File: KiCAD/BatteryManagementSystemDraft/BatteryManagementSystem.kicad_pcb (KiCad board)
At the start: 2 copper layers, 237.5 x 165 mm, 368 parts, among them J2 Conn_01x07_Male, J5 Conn_01x07_Male, J6 Conn_01x07_Male, Q1 Q_NMOS_GDS, Q2 NMOS_PowerPak_SO8, Q3 NMOS_PowerPak_SO8, Q4 NMOS_PowerPak_SO8, Q5 NMOS_PowerPak_SO8, T1 750311880, U1 750312504, U2 LTC3300HLXE-2#PBF, U3 LTC6804HG-1#PBF, U4 LTC6820IMS#PBF, U5 BQ79606APHPTQ1

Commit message: Updated Kicad Files
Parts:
- removed the C1 at (57.9, 160.4)
- removed the C1 at (57.9, 170.9)
- removed the C1 at (57.9, 139.6)
- removed the C1 at (58.0, 181.2)
- removed the C1 at (57.9, 129.2)
- removed the C1 at (57.9, 150.0)
- removed the C10 at (141.3, 92.0)
- removed the C10 at (141.3, 118.7)
- removed the C10 at (141.3, 171.1)
- removed the C10 at (141.3, 65.1)
- removed the C10 at (141.3, 145.2)
- removed the C10 at (141.3, 37.9)
- removed the C11 at (134.5, 52.4)
- removed the C11 at (134.5, 106.0)
- removed the C11 at (134.5, 79.3)
- removed the C11 at (134.5, 132.5)
- removed the C11 at (134.5, 158.4)
- removed the C11 at (134.5, 25.2)
- removed the C12 at (141.9, 52.4)
- removed the C12 at (141.9, 106.0)
- removed the C12 at (141.9, 79.3)
- removed the C12 at (141.9, 132.5)
- removed the C12 at (141.9, 158.4)
- removed the C12 at (141.9, 25.2)
- removed the C13 at (138.2, 79.3)
- removed the C13 at (138.2, 52.4)
- removed the C13 at (138.2, 106.0)
- removed the C13 at (138.2, 158.4)
- removed the C13 at (138.2, 132.5)
- removed the C13 at (138.2, 25.2)
- removed the C14 at (222.3, 85.8)
- removed the C14 at (199.4, 102.2)
- removed the C14 at (222.3, 118.2)
- removed the C14 at (199.4, 134.7)
- removed the C14 at (222.3, 152.1)
- removed the C14 at (199.4, 168.4)
- removed the C15 at (222.3, 89.2)
- removed the C15 at (199.4, 105.6)
- removed the C15 at (222.3, 121.6)
- removed the C15 at (199.4, 138.1)
- removed the C15 at (222.3, 155.5)
- removed the C15 at (199.4, 171.8)
- removed the C16 at (222.3, 92.7)
- removed the C16 at (199.4, 109.0)
- removed the C16 at (222.3, 125.0)
- removed the C16 at (199.4, 141.6)
- removed the C16 at (222.3, 159.0)
- removed the C16 at (199.4, 175.2)
- removed the C17 at (224.7, 97.2)
- removed the C17 at (201.8, 113.6)
- removed the C17 at (224.7, 129.6)
- removed the C17 at (201.8, 146.1)
- removed the C17 at (224.7, 163.5)
- removed the C17 at (201.8, 179.8)
- removed the C18 at (238.4, 94.2)
- removed the C18 at (215.5, 110.6)
- removed the C18 at (238.4, 126.6)
- removed the C18 at (215.5, 143.1)
- removed the C18 at (238.4, 160.5)
- removed the C18 at (215.5, 176.7)
- removed the C19 at (222.8, 80.5)
- removed the C19 at (199.9, 96.9)
- removed the C19 at (222.8, 112.9)
- removed the C19 at (199.9, 129.4)
- removed the C19 at (222.8, 146.8)
- removed the C19 at (199.9, 163.0)
- removed the C2 at (52.6, 129.1)
- removed the C2 at (52.6, 170.8)
- removed the C2 at (52.7, 181.2)
- removed the C2 at (52.6, 150.0)
- removed the C2 at (52.6, 160.4)
- removed the C2 at (52.6, 139.6)
- removed the C20 at (237.4, 91.0)
- removed the C20 at (214.5, 107.4)
- removed the C20 at (237.4, 123.4)
- removed the C20 at (214.5, 139.9)
- removed the C20 at (237.4, 157.3)
- removed the C20 at (214.5, 173.6)
- removed the C21 at (241.5, 91.5)
- removed the C21 at (218.6, 107.9)
- removed the C21 at (241.5, 123.9)
- removed the C21 at (218.6, 140.4)
- removed the C21 at (241.5, 157.8)
- removed the C21 at (218.6, 174.1)
- removed the C22 at (241.5, 84.4)
- removed the C22 at (218.6, 100.8)
- removed the C22 at (241.5, 116.8)
- removed the C22 at (218.6, 133.3)
- removed the C22 at (241.5, 150.7)
- removed the C22 at (218.6, 167.0)
- removed the C23 at (241.5, 88.0)
- removed the C23 at (218.6, 104.3)
- removed the C23 at (241.5, 120.3)
- removed the C23 at (218.6, 136.9)
- removed the C23 at (241.5, 154.3)
- removed the C23 at (218.6, 170.5)
- removed the C3 at (58.5, 126.4)
- removed the C3 at (58.5, 136.8)
- removed the C3 at (58.5, 157.7)
- removed the C3 at (58.5, 178.4)
- removed the C3 at (58.5, 147.3)
- removed the C3 at (58.5, 168.1)
- removed the C4 at (121.1, 46.3)
- removed the C4 at (121.1, 73.4)
- removed the C4 at (121.1, 153.6)
- removed the C4 at (121.1, 100.4)
- removed the C4 at (121.1, 127.0)
- removed the C4 at (121.1, 179.5)
- removed the C5 at (117.5, 73.4)
- removed the C5 at (117.5, 179.5)
- removed the C5 at (117.5, 100.4)
- removed the C5 at (117.5, 127.0)
- removed the C5 at (117.5, 153.6)
- removed the C5 at (117.5, 46.3)
- removed the C6 at (114.0, 73.4)
- removed the C6 at (114.0, 100.4)
- removed the C6 at (114.0, 153.6)
- removed the C6 at (114.0, 127.0)
- removed the C6 at (114.0, 179.5)
- removed the C6 at (114.0, 46.3)
- removed the C7 at (110.3, 50.3)
- removed the C7 at (110.3, 77.3)
- removed the C7 at (110.3, 103.9)
- removed the C7 at (110.3, 130.5)
- removed the C7 at (110.3, 156.4)
- removed the C7 at (110.3, 23.2)
- removed the C8 at (112.8, 64.3)
- removed the C8 at (112.8, 91.2)
- removed the C8 at (112.8, 117.9)
- removed the C8 at (112.8, 144.4)
- removed the C8 at (112.8, 170.3)
- removed the C8 at (112.8, 37.1)
- removed the C9 at (135.4, 69.9)
- removed the C9 at (135.4, 123.5)
- removed the C9 at (135.4, 96.8)
- removed the C9 at (135.4, 150.0)
- removed the C9 at (135.4, 175.9)
- removed the C9 at (135.4, 42.7)
- removed the D1 at (54.9, 139.7)
- removed the D1 at (55.0, 181.3)
- removed the D1 at (54.9, 160.5)
- removed the D1 at (54.9, 129.3)
- removed the D1 at (54.9, 150.1)
- removed the D1 at (54.9, 170.9)
- removed the D2 at (112.4, 94.9)
- removed the D2 at (112.4, 174.0)
- removed the D2 at (112.4, 148.1)
- removed the D2 at (112.4, 40.8)
- removed the D2 at (112.4, 121.6)
- removed the D2 at (112.4, 68.0)
- removed the D3 at (104.9, 57.2)
- removed the D3 at (104.9, 163.2)
- removed the D3 at (104.9, 110.8)
- removed the D3 at (104.9, 84.1)
- removed the D3 at (104.9, 137.3)
- removed the D3 at (104.9, 30.0)
- removed the D4 at (112.8, 59.5)
- removed the D4 at (112.8, 86.4)
- removed the D4 at (112.8, 165.5)
- removed the D4 at (112.8, 113.1)
- removed the D4 at (112.8, 139.6)
- removed the D4 at (112.8, 32.3)
- removed the D5 at (135.4, 92.0)
- removed the D5 at (135.4, 37.9)
- removed the D5 at (135.4, 171.1)
- removed the D5 at (135.4, 145.2)
- removed the D5 at (135.4, 118.7)
- removed the D5 at (135.4, 65.1)
- removed the D6 at (222.5, 92.7)
- removed the D6 at (199.7, 109.0)
- removed the D6 at (222.5, 125.0)
- removed the D6 at (199.7, 141.6)
- removed the D6 at (222.5, 159.0)
- removed the D6 at (199.7, 175.2)
- removed the D7 at (224.8, 96.0)
- removed the D7 at (201.9, 112.3)
- removed the D7 at (224.8, 128.3)
- removed the D7 at (201.9, 144.9)
- removed the D7 at (224.8, 162.3)
- removed the D7 at (201.9, 178.5)
- removed the D8 at (232.6, 90.5)
- removed the D8 at (209.7, 106.9)
- removed the D8 at (232.6, 122.9)
- removed the D8 at (209.7, 139.4)
- removed the D8 at (232.6, 156.8)
- removed the D8 at (209.7, 173.1)
- removed the D9 at (232.6, 87.7)
- removed the D9 at (209.7, 104.1)
- removed the D9 at (232.6, 120.1)
- removed the D9 at (209.7, 136.6)
- removed the D9 at (232.6, 154.0)
- removed the D9 at (209.7, 170.3)
- removed J5, J6: Conn_01x07_Male, Connector_PinHeader_2.54mm:PinHeader_1x07_P2.54mm_Horizontal
- removed the Q1 at (53.5, 133.4)
- removed the Q1 at (53.5, 143.9)
- removed the Q1 at (53.6, 175.0)
- removed the Q1 at (53.5, 154.3)
- removed the Q1 at (53.5, 123.0)
- removed the Q1 at (53.5, 164.7)
- removed the Q2 at (112.6, 55.2)
- removed the Q2 at (112.6, 82.1)
- removed the Q2 at (112.6, 108.8)
- removed the Q2 at (112.6, 135.3)
- removed the Q2 at (112.6, 161.2)
- removed the Q2 at (112.6, 28.0)
- removed the Q3 at (135.5, 87.8)
- removed the Q3 at (135.5, 60.9)
- removed the Q3 at (135.5, 114.5)
- removed the Q3 at (135.5, 33.7)
- removed the Q3 at (135.5, 166.9)
- removed the Q3 at (135.5, 141.0)
- removed the Q4 at (232.1, 97.9)
- removed the Q4 at (209.2, 114.3)
- removed the Q4 at (232.1, 130.3)
- removed the Q4 at (209.2, 146.8)
- removed the Q4 at (232.1, 164.2)
- removed the Q4 at (209.2, 180.4)
- removed the Q5 at (230.1, 80.0)
- removed the Q5 at (207.2, 96.3)
- removed the Q5 at (230.1, 112.3)
- removed the Q5 at (207.2, 128.9)
- removed the Q5 at (230.1, 146.3)
- removed the Q5 at (207.2, 162.5)
- removed the R1 at (44.3, 125.9)
- removed the R1 at (44.3, 157.2)
- removed the R1 at (44.3, 136.3)
- removed the R1 at (44.3, 177.9)
- removed the R1 at (44.3, 146.7)
- removed the R1 at (44.3, 167.6)
- removed the R10 at (141.8, 88.6)
- removed the R10 at (141.8, 115.2)
- removed the R10 at (141.8, 167.7)
- removed the R10 at (141.8, 34.5)
- removed the R10 at (141.8, 141.8)
- removed the R10 at (141.8, 61.6)
- removed the R11 at (139.1, 92.0)
- removed the R11 at (139.1, 37.9)
- removed the R11 at (139.1, 118.7)
- removed the R11 at (139.1, 171.1)
- removed the R11 at (139.1, 145.2)
- removed the R11 at (139.1, 65.1)
- removed the R12 at (138.2, 83.7)
- removed the R12 at (138.2, 136.9)
- removed the R12 at (138.2, 29.6)
- removed the R12 at (138.2, 110.4)
- removed the R12 at (138.2, 162.9)
- removed the R12 at (138.2, 56.8)
- removed the R13 at (227.3, 96.0)
- removed the R13 at (204.4, 112.3)
- removed the R13 at (227.3, 128.3)
- removed the R13 at (204.4, 144.9)
- removed the R13 at (227.3, 162.3)
- removed the R13 at (204.4, 178.5)
- removed the R14 at (227.3, 97.2)
- removed the R14 at (204.4, 113.6)
- removed the R14 at (227.3, 129.6)
- removed the R14 at (204.4, 146.1)
- removed the R14 at (227.3, 163.5)
- removed the R14 at (204.4, 179.8)
- removed the R15 at (225.8, 99.3)
- removed the R15 at (203.0, 115.7)
- removed the R15 at (225.8, 131.7)
- removed the R15 at (203.0, 148.2)
- removed the R15 at (225.8, 165.6)
- removed the R15 at (203.0, 181.8)
- removed the R16 at (238.4, 96.2)
- removed the R16 at (215.5, 112.6)
- removed the R16 at (238.4, 128.6)
- removed the R16 at (215.5, 145.1)
- removed the R16 at (238.4, 162.5)
- removed the R16 at (215.5, 178.8)
- removed the R17 at (224.9, 80.5)
- removed the R17 at (202.1, 96.9)
- removed the R17 at (224.9, 112.9)
- removed the R17 at (202.1, 129.4)
- removed the R17 at (224.9, 146.8)
- removed the R17 at (202.1, 163.0)
- removed the R18 at (237.6, 87.7)
- removed the R18 at (214.8, 104.1)
- removed the R18 at (237.6, 120.1)
- removed the R18 at (214.8, 136.6)
- removed the R18 at (237.6, 154.0)
- removed the R18 at (214.8, 170.3)
- removed the R19 at (237.4, 89.7)
- removed the R19 at (214.6, 106.1)
- removed the R19 at (237.4, 122.1)
- removed the R19 at (214.6, 138.6)
- removed the R19 at (237.4, 156.0)
- removed the R19 at (214.6, 172.3)
- removed the R2 at (56.7, 160.4)
- removed the R2 at (56.7, 170.9)
- removed the R2 at (56.7, 139.6)
- removed the R2 at (56.7, 150.0)
- removed the R2 at (56.7, 181.2)
- removed the R2 at (56.7, 129.2)
- removed the R20 at (235.0, 81.9)
- removed the R20 at (212.1, 98.3)
- removed the R20 at (235.0, 114.3)
- removed the R20 at (212.1, 130.8)
- removed the R20 at (235.0, 148.2)
- removed the R20 at (212.1, 164.4)
- removed the R3 at (53.4, 136.6)
- removed the R3 at (53.4, 126.2)
- removed the R3 at (53.5, 178.2)
- removed the R3 at (53.4, 157.4)
- removed the R3 at (53.4, 167.8)
- removed the R3 at (53.4, 147.0)
- removed the R4 at (56.7, 147.3)
- removed the R4 at (56.7, 178.4)
- removed the R4 at (56.7, 126.4)
- removed the R4 at (56.7, 136.8)
- removed the R4 at (56.7, 157.7)
- removed the R4 at (56.7, 168.1)
- removed the R5 at (107.5, 84.1)
- removed the R5 at (107.5, 163.2)
- removed the R5 at (107.5, 137.3)
- removed the R5 at (107.5, 110.8)
- removed the R5 at (107.5, 30.0)
- removed the R5 at (107.5, 57.2)
- removed the R6 at (110.3, 51.6)
- removed the R6 at (110.3, 78.5)
- removed the R6 at (110.3, 105.2)
- removed the R6 at (110.3, 157.6)
- removed the R6 at (110.3, 131.7)
- removed the R6 at (110.3, 24.4)
- removed the R7 at (106.3, 81.6)
- removed the R7 at (106.3, 54.6)
- removed the R7 at (106.3, 108.2)
- removed the R7 at (106.3, 134.8)
- removed the R7 at (106.3, 27.5)
- removed the R7 at (106.3, 160.7)
- removed the R8 at (112.8, 88.9)
- removed the R8 at (112.8, 62.0)
- removed the R8 at (112.8, 168.1)
- removed the R8 at (112.8, 115.6)
- removed the R8 at (112.8, 34.8)
- removed the R8 at (112.8, 142.2)
- removed the R9 at (135.4, 67.7)
- removed the R9 at (135.4, 147.9)
- removed the R9 at (135.4, 121.3)
- removed the R9 at (135.4, 173.8)
- removed the R9 at (135.4, 40.6)
- removed the R9 at (135.4, 94.7)
- removed T**, T1 (x6): 750311880, KICAD Components:750311880
- removed the U1 at (124.4, 88.1)
- removed the U1 at (124.4, 114.7)
- removed the U1 at (124.4, 141.3)
- removed the U1 at (124.4, 33.9)
- removed the U1 at (124.4, 167.2)
- removed the U1 at (124.4, 61.1)
- removed the U1 at (296.1, 170.6)
- removed the U2 at (152.5, 92.5)
- removed the U2 at (152.5, 107.5)
- removed the U2 at (257.5, 140.0)
- removed the U2 at (257.5, 125.0)
- removed the U3 at (152.5, 122.5)
- removed the U3 at (257.5, 155.0)
- removed the U4 at (152.5, 135.0)
- removed the U4 at (257.5, 167.5)
- added C1: 2.2uF 10V, Capacitor_SMD:C_0603_1608Metric, F.Cu at (129.2, 98.8)
- added C10: 1uF, Capacitor_SMD:C_0805_2012Metric, F.Cu at (113.5, 60.5)
- added C11: 1uF, Capacitor_SMD:C_0805_2012Metric, F.Cu at (122.4, 60.5)
- added C12: 2.2uF 10V, Capacitor_SMD:C_0603_1608Metric, F.Cu at (140.9, 111.9)
- added C13: 2.2uF 10V, Capacitor_SMD:C_0603_1608Metric, F.Cu at (140.9, 97.6)
- added C14: 2.2uF 10V, Capacitor_SMD:C_0603_1608Metric, F.Cu at (140.9, 100.8)
- added C15: 1nF, Capacitor_SMD:C_0603_1608Metric, F.Cu at (116.3, 85.2)
- added C16: 1nF, Capacitor_SMD:C_0603_1608Metric, F.Cu at (116.0, 96.2)
- added C17: 1nF, Capacitor_SMD:C_0603_1608Metric, F.Cu at (116.0, 106.5)
- added C18: 1nF, Capacitor_SMD:C_0603_1608Metric, F.Cu at (115.9, 117.0)
- added C19: 1nF, Capacitor_SMD:C_0603_1608Metric, F.Cu at (116.0, 127.6)
- added C2: 0.33uF, Capacitor_SMD:C_0805_2012Metric, F.Cu at (88.6, 59.3)
- added C20: 1nF, Capacitor_SMD:C_0603_1608Metric, F.Cu at (128.9, 127.9)
- added C21: 1uF, Capacitor_SMD:C_0603_1608Metric, F.Cu at (118.6, 80.7)
- added C22: 1uF, Capacitor_SMD:C_0603_1608Metric, F.Cu at (118.3, 91.7)
- added C23: 1uF, Capacitor_SMD:C_0603_1608Metric, F.Cu at (118.3, 102.1)
- added C24: 1uF, Capacitor_SMD:C_0603_1608Metric, F.Cu at (118.3, 112.6)
- added C25: 1uF, Capacitor_SMD:C_0603_1608Metric, F.Cu at (118.4, 123.1)
- added C26: 1uF, Capacitor_SMD:C_0603_1608Metric, F.Cu at (124.5, 125.5)
- added C27: 1uF, Capacitor_SMD:C_0603_1608Metric, F.Cu at (117.0, 77.5)
- added C28: 1uF, Capacitor_SMD:C_0603_1608Metric, F.Cu at (117.5, 89.3)
- added C29: 1uF, Capacitor_SMD:C_0603_1608Metric, F.Cu at (117.5, 99.6)
- added C3: 2.2uF 10V, Capacitor_SMD:C_0603_1608Metric, F.Cu at (127.6, 98.8)
- added C30: 1uF, Capacitor_SMD:C_0603_1608Metric, F.Cu at (117.4, 110.1)
- added C31: 1uF, Capacitor_SMD:C_0603_1608Metric, F.Cu at (117.5, 120.7)
- added C32: 1uF, Capacitor_SMD:C_0603_1608Metric, F.Cu at (122.1, 126.4)
- added C33: 470nF 16V, Capacitor_SMD:C_0603_1608Metric, F.Cu at (130.6, 124.6)
- added C34: 100nF 10V, Capacitor_SMD:C_0603_1608Metric, F.Cu at (126.9, 93.4)
- added C35: 10uF 10V, Capacitor_SMD:C_0603_1608Metric, F.Cu at (126.9, 90.3)
- added C36: 100nF 10V, Capacitor_SMD:C_0603_1608Metric, F.Cu at (135.9, 85.5)
- added C37: 0.1uF, Capacitor_SMD:C_0603_1608Metric, F.Cu at (124.4, 79.4)
- added C38: 100nF 10V, Capacitor_SMD:C_0603_1608Metric, F.Cu at (126.6, 75.6)
- added C39: 100nF 10V, Capacitor_SMD:C_0603_1608Metric, F.Cu at (124.4, 81.0)
- added C4: 2.2uF 10V, Capacitor_SMD:C_0603_1608Metric, F.Cu at (126.0, 98.8)
- added C5: 0.1uF, Capacitor_SMD:C_0805_2012Metric, F.Cu at (88.6, 66.3)
- added C6: 330nF 50V, Capacitor_SMD:C_0603_1608Metric, F.Cu at (124.3, 98.8)
- added C7: 100uF, Capacitor_SMD:CP_Elec_8x10.5, F.Cu at (95.9, 73.2)
- added C8: 330nF 50V, Capacitor_SMD:C_0603_1608Metric, F.Cu at (135.6, 98.8)
- added C9: 2.2uF 10V, Capacitor_SMD:C_0603_1608Metric, F.Cu at (140.9, 113.5)
- added D1: 1N6263W-7-F 1A, Diode_SMD:D_SOD-123, F.Cu at (108.3, 63.7)
- added D10: LED, LED_SMD:LED_0603_1608Metric, F.Cu at (130.0, 70.3)
- added D2: 1N6263W-7-F 1A, Diode_SMD:D_SOD-123, F.Cu at (116.9, 63.9)
- added D3: TVS_5.1V, Diode_SMD:D_SOD-323, F.Cu at (116.4, 83.3)
- added D4: TVS_5.1V, Diode_SMD:D_SOD-323, F.Cu at (116.0, 94.4)
- added D5: TVS_5.1V, Diode_SMD:D_SOD-323, F.Cu at (116.0, 104.7)
- added D6: TVS_5.1V, Diode_SMD:D_SOD-323, F.Cu at (116.0, 115.1)
- added D7: TVS_5.1V, Diode_SMD:D_SOD-323, F.Cu at (116.1, 125.7)
- added D8: TVS_5.1V, Diode_SMD:D_SOD-323, F.Cu at (127.1, 127.8)
- added D9: LED, LED_SMD:LED_0603_1608Metric, F.Cu at (131.6, 70.4)
- added J1: Conn_01x07_Male, Connector_PinHeader_2.54mm:PinHeader_1x07_P2.54mm_Vertical, F.Cu at (91.5, 117.0)
- added J3: Screw_Terminal_01x02, TerminalBlock:TerminalBlock_bornier-2_P5.08mm, F.Cu at (134.8, 47.8)
- added J4: Conn_01x04_Male, Connector_PinHeader_2.54mm:PinHeader_1x04_P2.54mm_Vertical, F.Cu at (141.1, 91.3)
- added JP1: Jumper_2_Open, Connector_PinHeader_2.54mm:PinHeader_1x02_P2.54mm_Vertical, F.Cu at (141.1, 64.5)
- added JP2: Jumper_2_Open, Connector_PinHeader_2.54mm:PinHeader_1x02_P2.54mm_Vertical, F.Cu at (141.1, 79.8)
- added JP3: Jumper_2_Open, Connector_PinHeader_2.54mm:PinHeader_1x02_P2.54mm_Vertical, F.Cu at (141.1, 73.4)
- added Q1: STB45N65M5 NMOS, Package_TO_SOT_SMD:TO-263-2, F.Cu at (104.7, 50.6)
- added Q2: STB45N65M5 NMOS, Package_TO_SOT_SMD:TO-263-2, F.Cu at (121.9, 50.7)
- added Q3: CSD16342Q5A, Package_TO_SOT_SMD:TDSON-8-1, F.Cu at (111.4, 82.7)
- added Q4: CSD16342Q5A, Package_TO_SOT_SMD:TDSON-8-1, F.Cu at (111.4, 93.7)
- added Q5: CSD16342Q5A, Package_TO_SOT_SMD:TDSON-8-1, F.Cu at (111.4, 103.6)
- added Q6: CSD16342Q5A, Package_TO_SOT_SMD:TDSON-8-1, F.Cu at (111.4, 114.0)
- added Q7: CSD16342Q5A, Package_TO_SOT_SMD:TDSON-8-1, F.Cu at (111.4, 124.5)
- added Q8: CSD16342Q5A, Package_TO_SOT_SMD:TDSON-8-1, F.Cu at (111.4, 134.3)
- added R1: 100R, Resistor_SMD:R_0603_1608Metric, F.Cu at (122.7, 98.8)
- added R10: 100k, Resistor_SMD:R_0603_1608Metric, F.Cu at (111.8, 60.7)
- added R11: 100R, Resistor_SMD:R_0603_1608Metric, F.Cu at (110.2, 60.7)
- added R12: 100k, Resistor_SMD:R_0603_1608Metric, F.Cu at (130.7, 98.8)
- added R13: 100k, Resistor_SMD:R_0603_1608Metric, F.Cu at (140.9, 115.1)
- added R14: 100R, Resistor_SMD:R_0603_1608Metric, F.Cu at (119.0, 60.7)
- added R15: 10k, Resistor_SMD:R_0603_1608Metric, F.Cu at (140.9, 102.4)
- added R16: 10k, Resistor_SMD:R_0603_1608Metric, F.Cu at (140.9, 103.9)
- added R17: 10k, Resistor_SMD:R_0603_1608Metric, F.Cu at (140.9, 105.5)
- added R18: 10k, Resistor_SMD:R_0603_1608Metric, F.Cu at (140.9, 107.1)
- added R19: 10k, Resistor_SMD:R_0603_1608Metric, F.Cu at (140.9, 108.7)
- added R2: 100k, Resistor_SMD:R_0603_1608Metric, F.Cu at (113.7, 70.7)
- added R20: 10k, Resistor_SMD:R_0603_1608Metric, F.Cu at (140.9, 110.3)
- added R21: 100k, Resistor_SMD:R_0603_1608Metric, F.Cu at (120.6, 60.7)
- added R22: 0R, Resistor_SMD:R_0603_1608Metric, F.Cu at (138.3, 92.1)
- added R23: 0R750, Package_TO_SOT_SMD:TO-252-2_TabPin1, F.Cu at (101.8, 82.9)
- added R24: 0R750, Package_TO_SOT_SMD:TO-252-2_TabPin1, F.Cu at (101.8, 93.9)
- added R25: 0R750, Package_TO_SOT_SMD:TO-252-2_TabPin1, F.Cu at (101.8, 103.8)
- added R26: 0R750, Package_TO_SOT_SMD:TO-252-2_TabPin1, F.Cu at (101.8, 114.2)
- added R27: 0R750, Package_TO_SOT_SMD:TO-252-2_TabPin1, F.Cu at (101.7, 124.7)
- added R28: 0R750, Package_TO_SOT_SMD:TO-252-2_TabPin1, F.Cu at (101.7, 134.5)
- added R29: 100R, Resistor_SMD:R_0603_1608Metric, F.Cu at (119.4, 78.4)
- added R3: 100k, Resistor_SMD:R_0603_1608Metric, F.Cu at (122.4, 70.7)
- added R30: 400R, Resistor_SMD:R_0603_1608Metric, F.Cu at (119.4, 76.7)
- added R31: 1k, Resistor_SMD:R_0603_1608Metric, F.Cu at (116.2, 81.5)
- added R32: 100R, Resistor_SMD:R_0603_1608Metric, F.Cu at (116.3, 86.8)
- added R33: 400R, Resistor_SMD:R_0603_1608Metric, F.Cu at (116.2, 79.8)
- added R34: 1k, Resistor_SMD:R_0603_1608Metric, F.Cu at (115.9, 92.5)
- added R35: 100R, Resistor_SMD:R_0603_1608Metric, F.Cu at (116.0, 97.8)
- added R36: 400R, Resistor_SMD:R_0603_1608Metric, F.Cu at (115.9, 90.9)
- added R37: 1k, Resistor_SMD:R_0603_1608Metric, F.Cu at (115.9, 102.9)
- added R38: 100R, Resistor_SMD:R_0603_1608Metric, F.Cu at (116.0, 108.1)
- added R39: 400R, Resistor_SMD:R_0603_1608Metric, F.Cu at (115.9, 101.2)
- added R4: 49R, Resistor_SMD:R_0805_2012Metric, F.Cu at (137.4, 98.6)
- added R40: 1k, Resistor_SMD:R_0603_1608Metric, F.Cu at (115.8, 113.3)
- added R41: 100R, Resistor_SMD:R_0603_1608Metric, F.Cu at (115.9, 118.6)
- added R42: 400R, Resistor_SMD:R_0603_1608Metric, F.Cu at (115.8, 111.7)
- added R43: 1k, Resistor_SMD:R_0603_1608Metric, F.Cu at (116.0, 123.9)
- added R44: 100R, Resistor_SMD:R_0603_1608Metric, F.Cu at (116.0, 129.2)
- added R45: 400R, Resistor_SMD:R_0603_1608Metric, F.Cu at (116.0, 122.2)
- added R46: 1k, Resistor_SMD:R_0603_1608Metric, F.Cu at (125.3, 128.0)
- added R47: 100R, Resistor_SMD:R_0603_1608Metric, F.Cu at (130.6, 127.9)
- added R48: 400R, Resistor_SMD:R_0603_1608Metric, F.Cu at (123.7, 128.0)
- added R49: 10k, Resistor_SMD:R_0603_1608Metric, F.Cu at (131.6, 73.5)
- added R5: 2R, Resistor_SMD:R_0805_2012Metric, F.Cu at (108.3, 68.0)
- added R50: 10k, Resistor_SMD:R_0603_1608Metric, F.Cu at (130.0, 73.5)
- added R51: 100k, Resistor_SMD:R_0603_1608Metric, F.Cu at (128.4, 73.5)
- added R6: 2R, Resistor_SMD:R_0805_2012Metric, F.Cu at (116.9, 68.1)
- added R7: 100k, Resistor_SMD:R_0603_1608Metric, F.Cu at (140.9, 99.2)
- added R8: 100k, Resistor_SMD:R_0603_1608Metric, F.Cu at (132.3, 98.8)
- added R9: 100k, Resistor_SMD:R_0603_1608Metric, F.Cu at (133.9, 98.8)
- added U1: L7812CD2T, Package_TO_SOT_SMD:TO-263-2, F.Cu at (98.0, 62.8)
- added U2: BQ79606APHPTQ1, KICAD Components:QFP50P900X900X120-49N, F.Cu at (131.1, 106.2)
- added U3: LM5109BMA, Package_SO:SOIC-8_3.9x4.9mm_P1.27mm, F.Cu at (112.2, 66.0)
- added U4: LM5109BMA, Package_SO:SOIC-8_3.9x4.9mm_P1.27mm, F.Cu at (121.0, 66.1)
- added U6: STM32L071KBTx, Package_QFP:LQFP-32_7x7mm_P0.8mm, F.Cu at (131.3, 80.6)
- J2: value Conn_01x07_Male -> Screw_Terminal_01x02; footprint Connector_PinHeader_2.54mm:PinHeader_1x07_P2.54mm_Horizontal -> TerminalBlock:TerminalBlock_bornier-2_P5.08mm
- U5: value BQ79606APHPTQ1 -> LD1117S33TR_SOT223; footprint KICAD Components:QFP50P900X900X120-49N -> Package_TO_SOT_SMD:SOT-223-3_TabPin2
- moved J2 125.4 mm to (91.5, 47.8), turned to 270 degrees
- moved U5 89.1 mm to (132.2, 91.3)
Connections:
- J2 pad 1: Net-(C1-Pad2) -> /+25V2
- J2 pad 2: CB1 -> GND
- U5 pad 1: Net-(U5-Pad1) -> GND
- U5 pad 2: Net-(U5-Pad2) -> /MCU/VCCDebug
- U5 pad 3: Net-(U5-Pad3) -> /VLDO
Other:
- board size 237.5 x 165 mm -> 59 x 96 mm
- board text removed: "Active Balancing"
- board text removed: "Passive Balancing"

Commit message: Layout Update
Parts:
- moved R50 17.0 mm to (138.0, 58.5), turned to 180 degrees
- moved D10 16.3 mm to (141.2, 58.5), turned to 180 degrees
- moved R49 14.8 mm to (138.0, 60.1), turned to 180 degrees
- moved D9 14.0 mm to (141.2, 60.1), turned to 180 degrees
- moved J3 7.50 mm to (140.0, 53.2), turned to 90 degrees
- moved C7 6.07 mm to (101.9, 74.4)
- moved C5 5.25 mm to (91.5, 70.7), turned to 0 degrees
- moved J2 5.16 mm to (91.1, 52.9), turned to 90 degrees
- moved C2 5.16 mm to (93.2, 57.0), turned to 180 degrees
- moved R13 4.25 mm to (140.9, 119.3)
- moved R15 4.25 mm to (140.9, 106.6)
- moved R18 4.25 mm to (140.9, 111.4)
- moved R20 4.25 mm to (140.9, 114.6)
- moved R7 4.25 mm to (140.9, 103.4)
- moved U2 4.25 mm to (131.1, 110.5)
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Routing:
- net /+25V2: track 0.00 -> 110.6 mm, vias 0 -> 9
- net /WAKEUP: track 0.00 -> 86.9 mm, vias 0 -> 2
- net /CELL0: track 0.00 -> 71.6 mm
- net /NFAULT: track 0.00 -> 63.5 mm, vias 0 -> 2
- net /BmsRX_McuTX: track 0.00 -> 57.5 mm, vias 0 -> 2
- net /VLDO: track 0.00 -> 56.9 mm, vias 0 -> 5
- net /BmsTX_McuRX: track 0.00 -> 53.7 mm, vias 0 -> 2
- net Net-(C14-Pad2): track 0.00 -> 48.8 mm, vias 0 -> 3
- net /BalancingCircuit/CB6: track 0.00 -> 46.8 mm
- net /BalancingCircuit/CB5: track 0.00 -> 42.1 mm
- net /CELL1: track 0.00 -> 41.3 mm
- net /BalancingCircuit/VC6: track 0.00 -> 41.1 mm
- net /BalancingCircuit/VC5: track 0.00 -> 39.2 mm, vias 0 -> 2
- net /BalancingCircuit/CB1: track 0.00 -> 36.7 mm
- net /DischargeEnable: track 0.00 -> 36.4 mm
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- added copper zone on F.Cu, net /+12V
- added copper zone on In2.Cu, net /+12V
- added copper zone on F.Cu, net /+25V2
- added copper zone on F.Cu, net /CELL0
- added copper zone on F.Cu, net /CELL1
- added copper zone on F.Cu, net /CELL2
- added copper zone on F.Cu, net /CELL3
- added copper zone on F.Cu, net /CELL4
- added copper zone on F.Cu, net /CELL5
- added copper zone on F.Cu, net /MCU/VCCDebug
- added copper zone on In2.Cu, net /MCU/VCCDebug
- added copper zone on F.Cu, net /VsCharge
- added copper zone on F.Cu, net GND
- added copper zone on In1.Cu, net GND
- added copper zone on F.Cu, net Net-(J3-Pad1)
- added copper zone on F.Cu, net Net-(Q3-Pad5)
- added copper zone on F.Cu, net Net-(Q4-Pad5)
- added copper zone on F.Cu, net Net-(Q5-Pad5)
- added copper zone on F.Cu, net Net-(Q6-Pad5)
- added copper zone on F.Cu, net Net-(Q7-Pad5)
- added copper zone on F.Cu, net Net-(Q8-Pad5)
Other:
- board size 59 x 96 mm -> 57 x 96 mm
- copper layers 2 -> 4

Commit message: Updated Layout
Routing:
- net Net-(J3-Pad1): vias 0 -> 29
- net GND: vias 43 -> 53
- net /VsCharge: vias 0 -> 9
- net /CELL4: vias 0 -> 5
- net /CELL3: vias 0 -> 5
- net /CELL2: vias 0 -> 5
- net /CELL1: vias 0 -> 5
- net /+25V2: vias 9 -> 32
- added copper zone on B.Cu, net GND
- added copper zone on In2.Cu, net GND
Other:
- outline, holes or cut-outs redrawn
- board text added: "+25V2"
- board text added: "+3V3"
- board text added: "Battery Managment System ICs: STM32L071KBTx & BQ79606APHPTQ1 Author: GM Date: 8.9.2021 Rev: 1.0"
- board text added: "C0"
- board text added: "C1"
- board text added: "C2"
- board text added: "C3"
- board text added: "C4"
- board text added: "C5"
- board text added: "C6"
- board text added: "EXTO1"
- board text added: "EXTO2"
- board text added: "GND"
- board text added: "LOAD/CHARGER"
- board text added: "RESET"
- board text added: "SWCLK"
- board text added: "SWDIO"

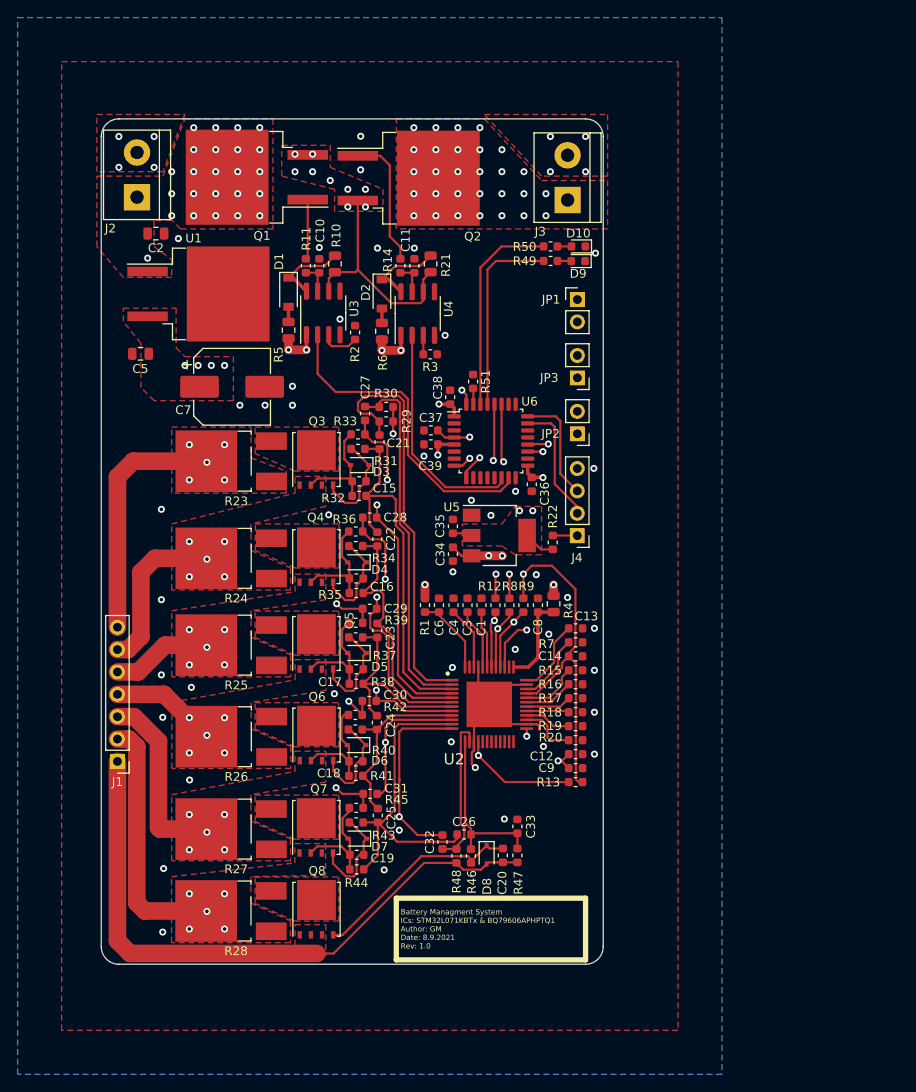
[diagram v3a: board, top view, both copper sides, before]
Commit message: Added Shunt Current Measurement
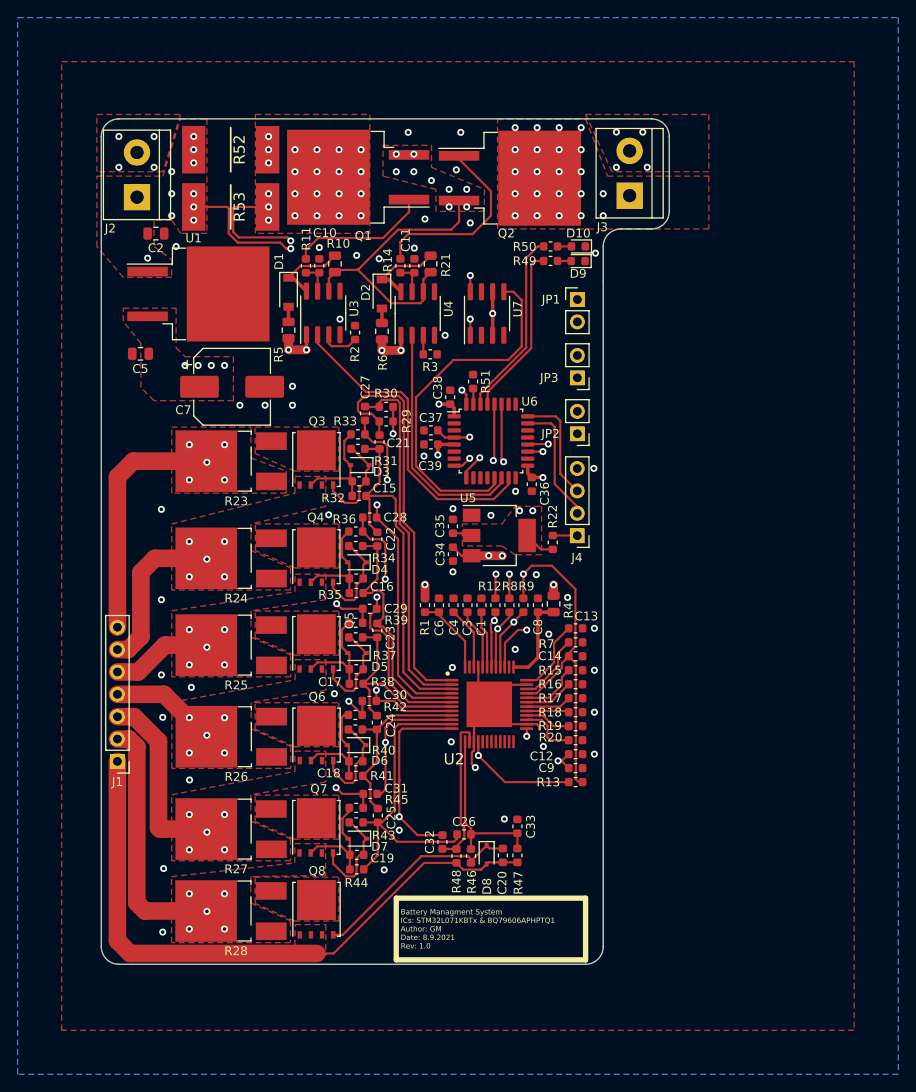
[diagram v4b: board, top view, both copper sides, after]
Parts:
- added R52: CSS2H-3920R-L200F, KICAD Components:RESC10052X130N, F.Cu at (101.7, 47.5)
- added R53: CSS2H-3920R-L200F, KICAD Components:RESC10052X130N, F.Cu at (101.7, 54.0)
- added U7: INA286, Package_SO:SOIC-8_3.9x4.9mm_P1.27mm, F.Cu at (130.8, 66.1)
- moved Q2 11.5 mm to (133.4, 50.7)
- moved Q1 11.5 mm to (116.2, 50.6)
- moved J3 7.06 mm to (147.0, 52.7)
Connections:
- net /MCU/VCCDebug renamed +3V3
- Q1 pad 2: /+25V2 -> Net-(Q1-Pad2)
- U6 pad 13: Net-(U6-Pad13) -> /MCU/Vcurrent
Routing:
- net Net-(Q1-Pad2): track 0.00 -> 44.5 mm, vias 0 -> 24
- net /MCU/Vcurrent: track 0.00 -> 41.0 mm
- net /+25V2: track 110.6 -> 150.1 mm, vias 32 -> 20
- net +3V3: track 14.6 -> 32.4 mm, vias 5 -> 6
- net Net-(Q1-Pad1): track 6.81 -> 16.2 mm
- net /VsCharge: track 25.7 -> 34.0 mm
- net Net-(Q2-Pad1): track 15.2 -> 21.7 mm
- net /MCU/ExtraIndicatorOutput: track 22.1 -> 19.5 mm
- net /MCU/PowerUpIndicatorOutput: track 23.7 -> 21.3 mm
- net /ChargeEnable: track 26.0 -> 27.6 mm
- net Net-(J3-Pad1): vias 29 -> 22
- net GND: vias 53 -> 57
- added copper zone on F.Cu, net Net-(Q1-Pad2)
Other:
- board size 57 x 96 mm -> 64.5 x 96 mm

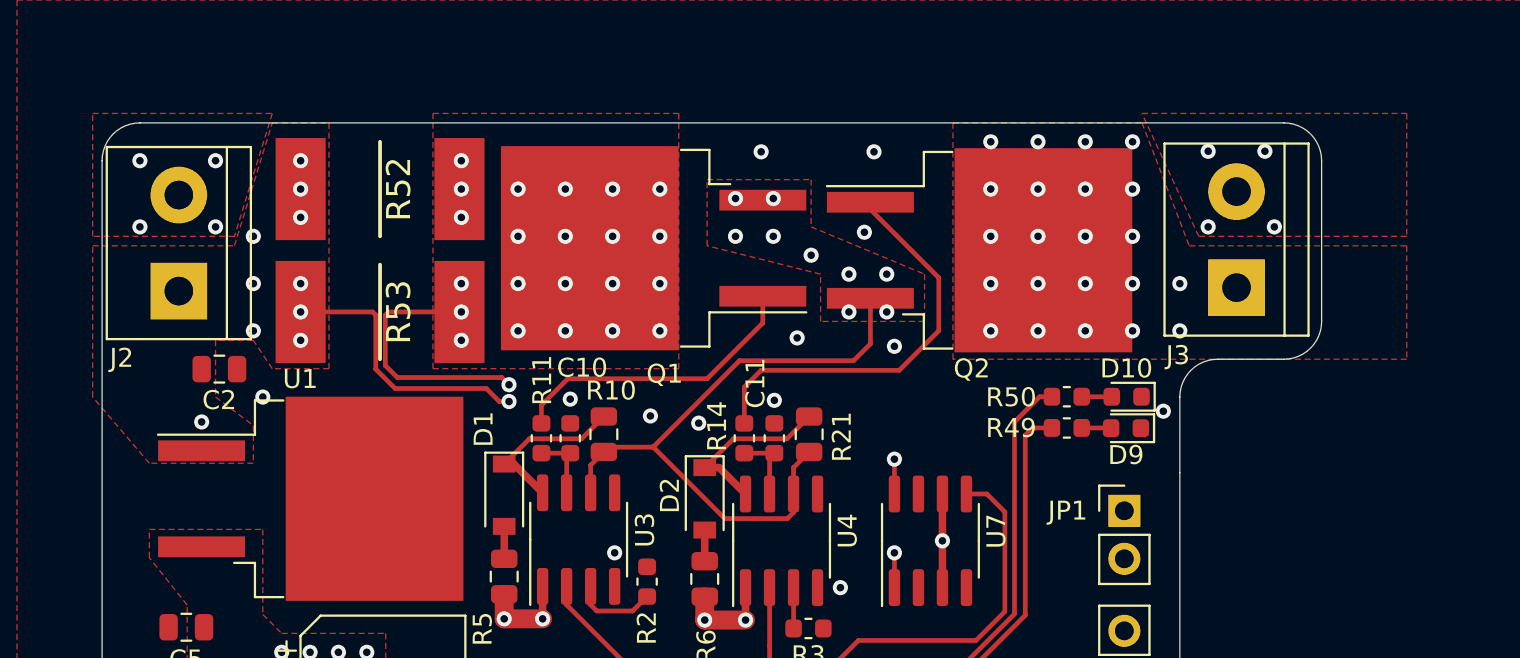
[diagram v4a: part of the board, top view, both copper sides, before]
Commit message: Layout main mosfet changes
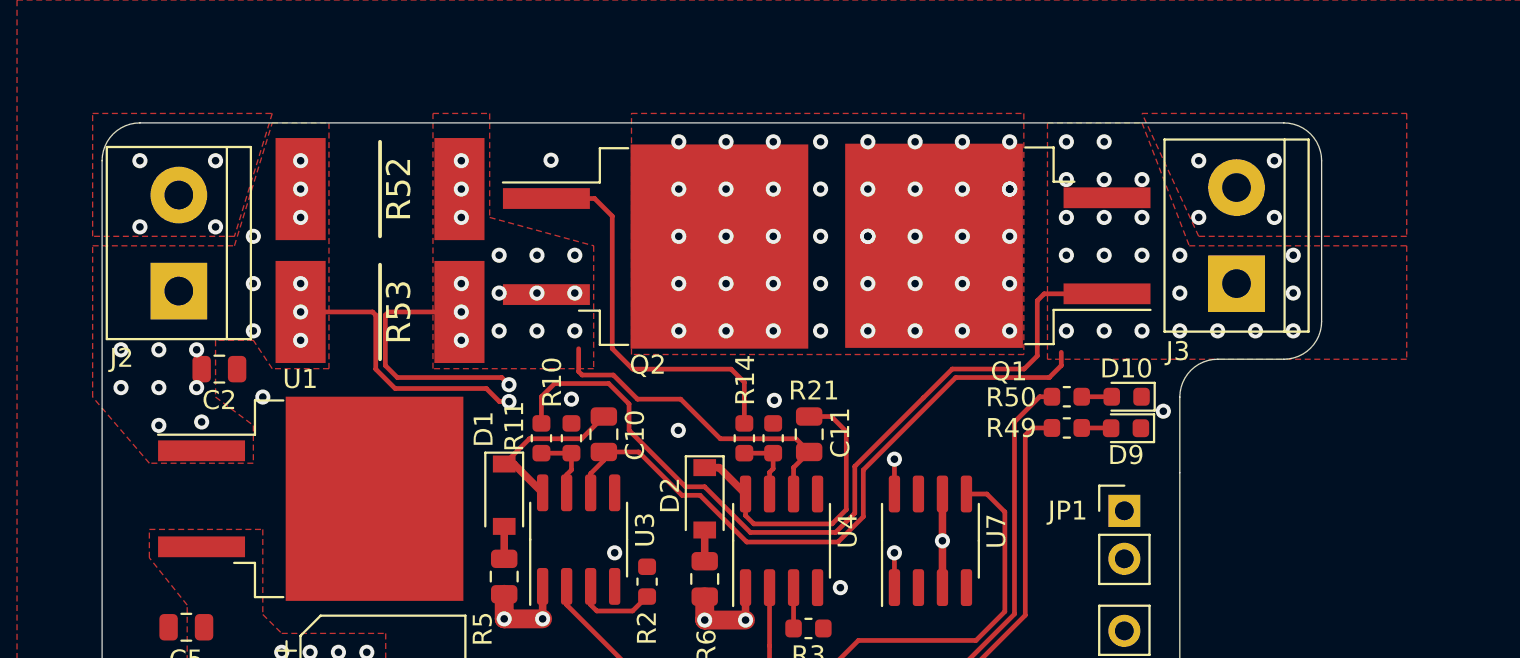
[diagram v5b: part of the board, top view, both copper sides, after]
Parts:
- moved Q1 18.2 mm to (134.4, 50.5)
- moved Q2 17.1 mm to (116.3, 50.5)
- moved R10 10.7 mm to (111.8, 60.7)
- moved R11 10.7 mm to (110.2, 60.7)
- moved R14 10.7 mm to (121.0, 60.7)
- moved R21 10.7 mm to (122.5, 60.7)
- moved J3 0.21 mm to (147.0, 52.5)
- renumbered R21 to R10, R14 to R11, R11 to R14, R10 to R21
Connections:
- C10 pad 1: /VsCharge -> /VsDischarge
- J3 pad 1: Net-(J3-Pad1) -> /VsDischarge
- Q1 pad 3: /VsCharge -> /VsDischarge
- Q2 pad 2: Net-(J3-Pad1) -> Net-(Q1-Pad2)
- R10 pad 2: /HOCharge -> /HODischarge
- R11 pad 1: /HOCharge -> /HODischarge
- R11 pad 2: Net-(Q2-Pad1) -> Net-(Q1-Pad1)
- R14 pad 1: /HODischarge -> /HOCharge
- R14 pad 2: Net-(Q1-Pad1) -> Net-(Q2-Pad1)
- R21 pad 2: /HODischarge -> /HOCharge
- R52 pad 2: Net-(Q1-Pad2) -> /VsCharge
- R53 pad 2: Net-(Q1-Pad2) -> /VsCharge
- U3 pad 6: /VsCharge -> /VsDischarge
- U7 pad 1: Net-(Q1-Pad2) -> /VsCharge
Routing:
- net Net-(Q1-Pad2): track 44.5 -> 0.38 mm, vias 24 -> 42
- net /VsDischarge: track 0.00 -> 34.6 mm, vias 0 -> 22
- net /VsCharge: track 34.0 -> 62.2 mm, vias 9 -> 17
- net Net-(Q1-Pad1): track 16.2 -> 44.1 mm
- net Net-(C11-Pad2): track 9.38 -> 16.1 mm
- net Net-(Q2-Pad1): track 21.7 -> 20.8 mm
- net Net-(J3-Pad1): vias 22 -> 0
- net GND: vias 57 -> 52
- net /+25V2: vias 20 -> 27
- added copper zone on F.Cu, net /VsDischarge
- removed copper zone on F.Cu, net Net-(J3-Pad1)
